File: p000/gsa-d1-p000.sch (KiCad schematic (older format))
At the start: 36 parts, among them J401 CONN-3, J402 CONN-2, J403 CONN-3, J404 CONN-2, U401 LM1876

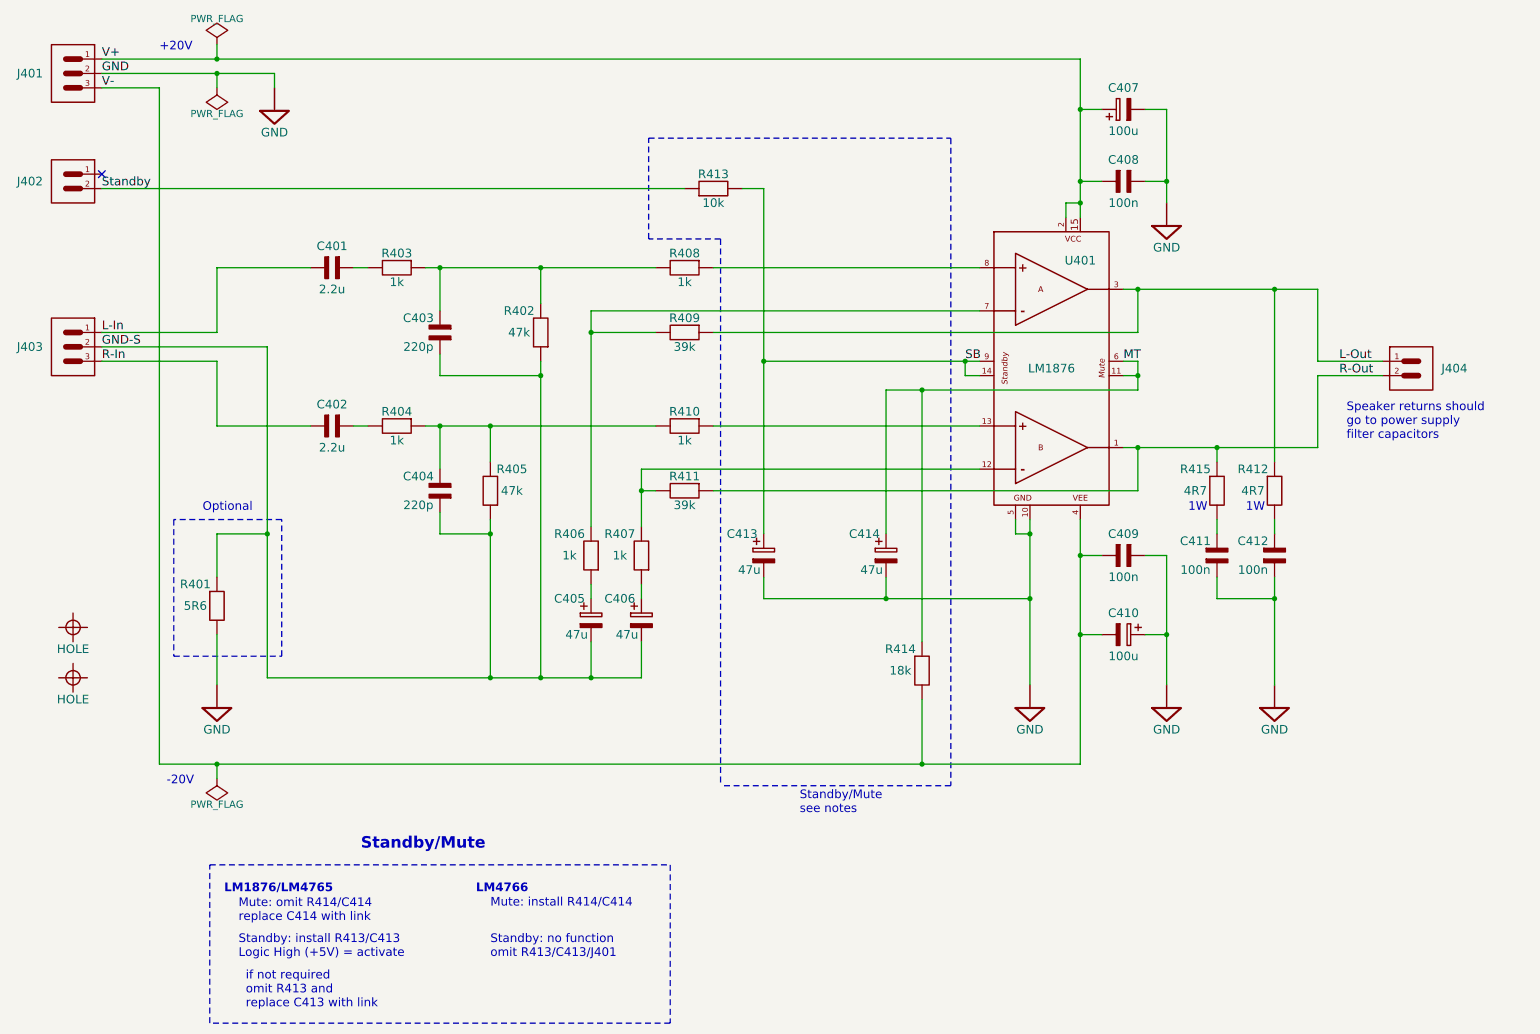
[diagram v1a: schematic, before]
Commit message: Reduce size of power supply PCB
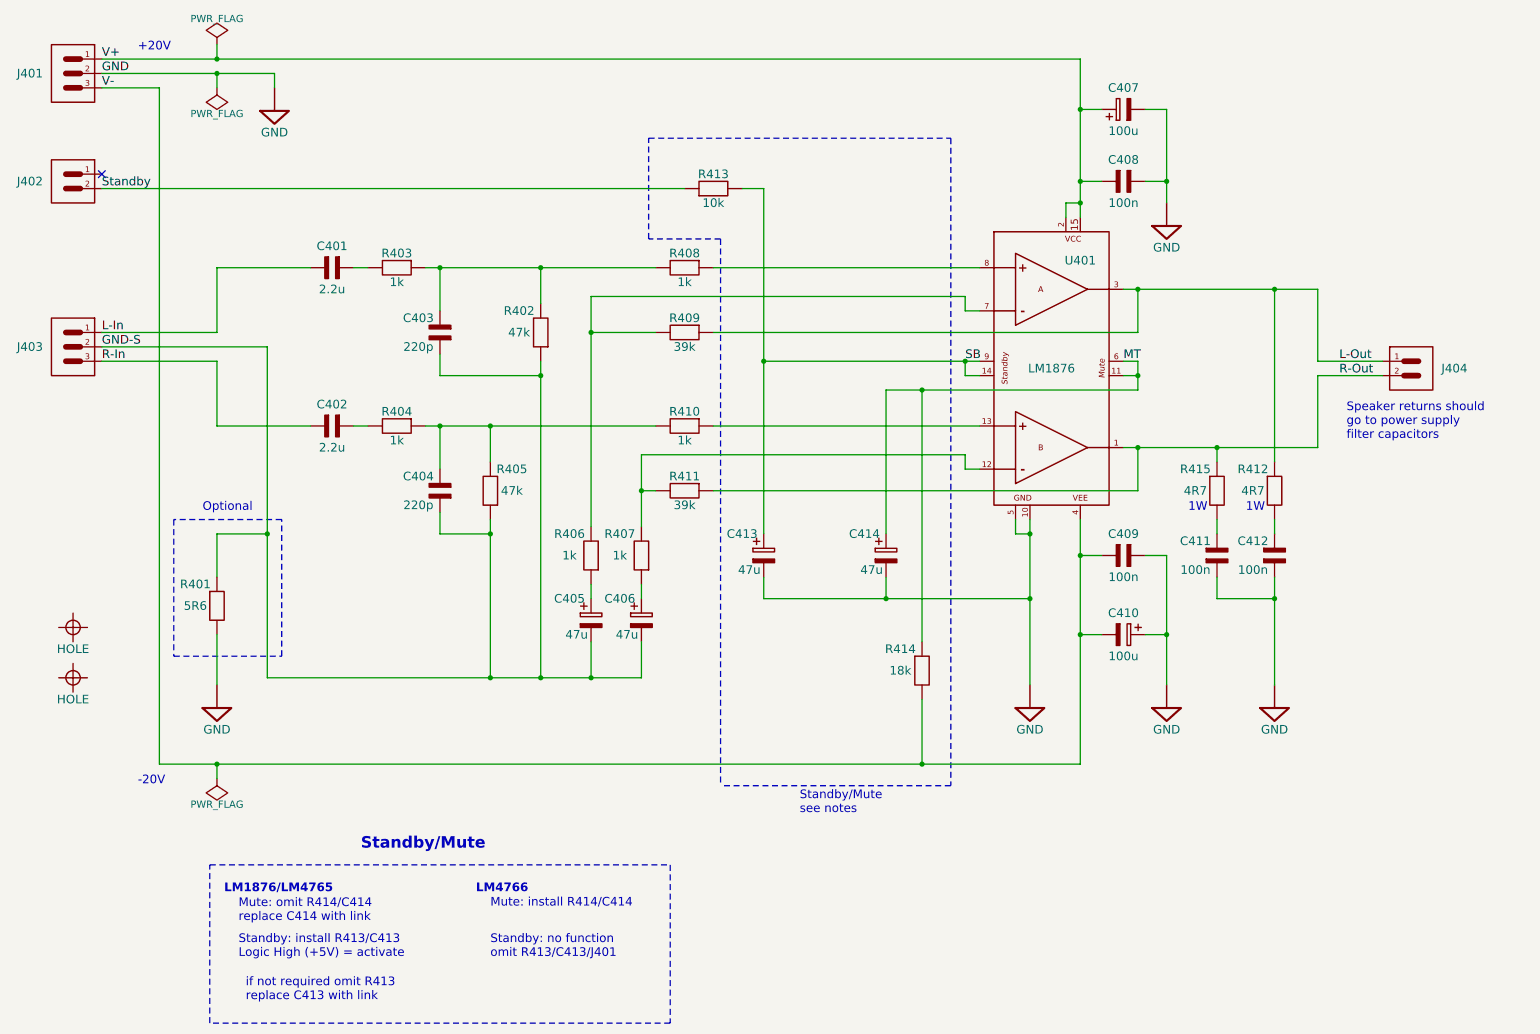
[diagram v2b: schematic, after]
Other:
- note added: "if not required omit R413\nreplace C413 with link"
- note removed: "if not required\nomit R413 and \nreplace C413 with link"
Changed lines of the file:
@@
 Text Notes 4050 6800 0    60   ~ 0
 Mute: install R414/C414
-Text Notes 2350 7500 0    60   ~ 0
-if not required\nomit R413 and \nreplace C413 with link
+Text Notes 2350 7450 0    60   ~ 0
+if not required omit R413\nreplace C413 with link
 Text Label 8450 3000 0    60   ~ 0
 MT
@@
 	-1   0    0    -1
 $EndComp
-Text Notes 1750 850  0    60   ~ 0
+Text Notes 1600 850  0    60   ~ 0
 +20V
-Text Notes 1800 5950 0    60   ~ 0
+Text Notes 1600 5950 0    60   ~ 0
 -20V
 Text Notes 2300 6900 0    60   ~ 0
@@
 	8550 3900 8550 3600
 Wire Wire Line
-	5100 3750 5100 4150
+	5100 3650 5100 4150
 Wire Wire Line
 	5200 3900 5100 3900
@@
 Connection ~ 4750 2800
 Wire Wire Line
-	4750 2650 4750 4150
+	4750 2550 4750 4150
 Wire Wire Line
 	4750 4550 4750 4650
@@
 	5600 2350 7450 2350
 Wire Wire Line
-	4750 2650 7450 2650
-Wire Wire Line
 	5600 3450 7450 3450
-Wire Wire Line
-	5100 3750 7450 3750
 Wire Wire Line
 	5600 2800 8550 2800
@@
 Text Notes 2050 4050 0    60   ~ 0
 Optional
+Wire Wire Line
+	4750 2550 7350 2550
+Wire Wire Line
+	7350 2550 7350 2650
+Wire Wire Line
+	7350 2650 7450 2650
+Wire Wire Line
+	5100 3650 7350 3650
+Wire Wire Line
+	7350 3650 7350 3750
+Wire Wire Line
+	7350 3750 7450 3750
 $EndSCHEMATC

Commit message: Updated to use KiCad v5
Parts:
- C401, C402, C403, C404, C408, C409, C411, C412: symbol CAP -> gsa:CAP
- C405, C406, C407, C410, C413, C414: symbol CAP-P -> gsa:CAP-P
- H401, H402: symbol HOLE -> gsa:HOLE
- J401, J403: symbol CONN-3 -> gsa:CONN-3
- J402, J404: symbol CONN-2 -> gsa:CONN-2
- R401, R402, R403, R404, R405, R406, R407, R408, R409, R410, R411, R412, R413, R414, R415: symbol RES -> gsa:RES
- U401: symbol LM1876 -> gsa:LM1876
